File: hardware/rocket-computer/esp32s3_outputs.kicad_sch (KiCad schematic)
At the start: 43 parts, among them J5 Conn_01x04, SW3 R-667995, U11 GD5F2GQ5UEYIGR, U13 W25Q128JVYIQ, U14 479480001, U15 ESP32-S3RH2, U29 TPS22810DRVR, Y1 ABS07-32.768KHZ-T, Y2 ECS-400-10-37B2-CKY-TR

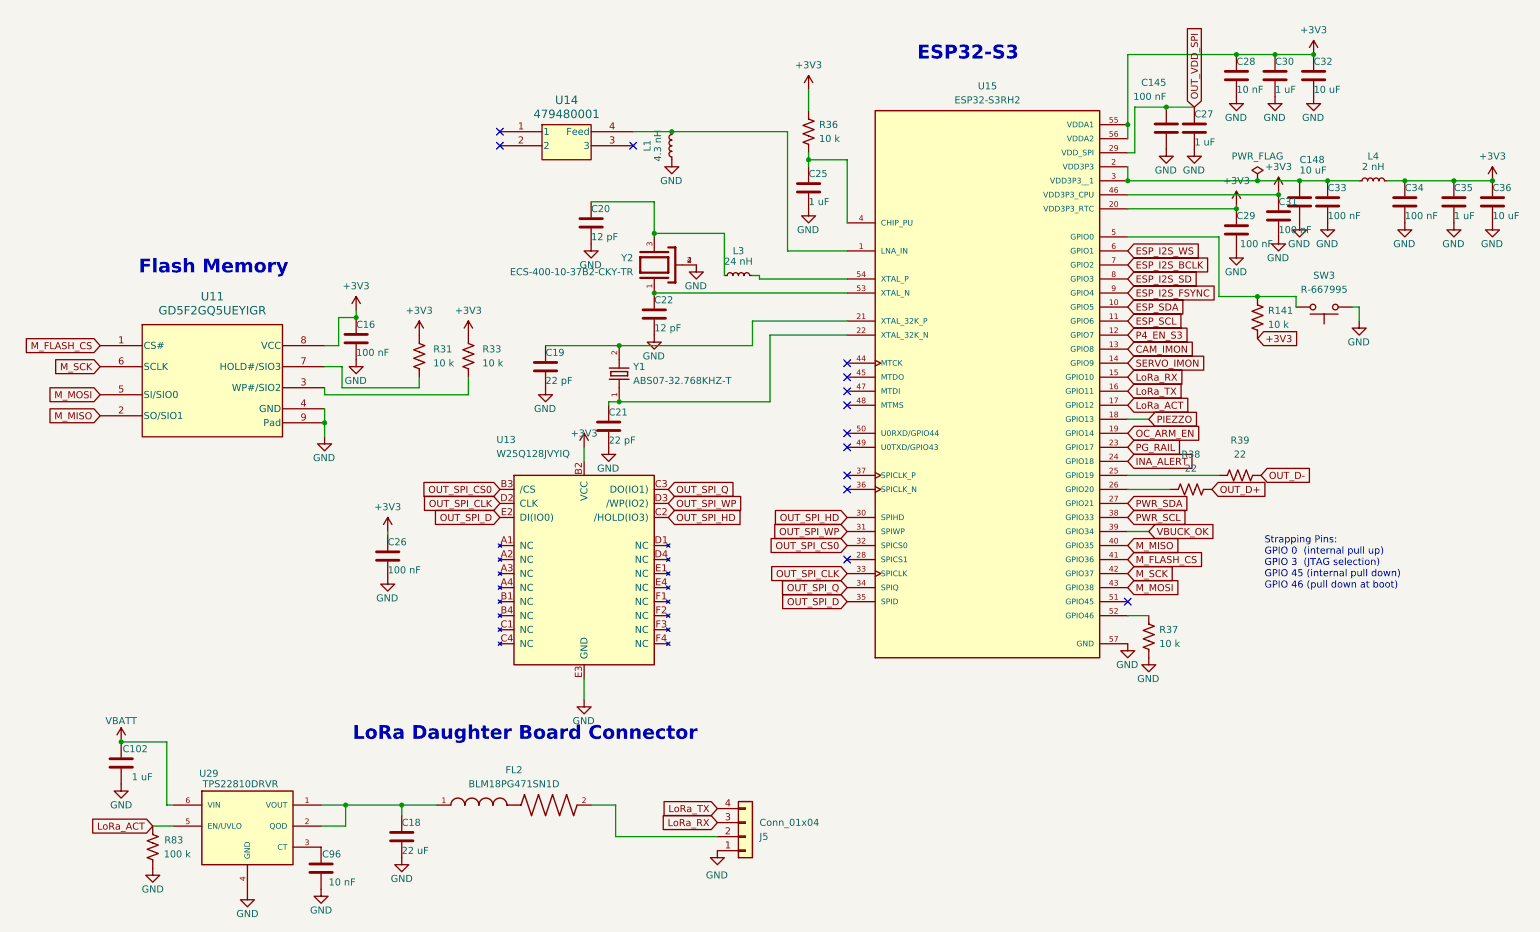
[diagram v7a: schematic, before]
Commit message: hardware(V10): chip antenna in place of the Molex part, buzzer removed, expansion header re-pinned, eight-layer board
Work in progress on the rocket-computer V10, committed so it is not lost. Schematic and
board; placement is under way and routing is not finished, so this is a snapshot of
work in progress rather than a releasable state.

Schematic, against the previous commit: 277 components and 279 nets become 275 and 274.

- The S3 radio front end moves to the mini's network: U22 AANI-CH-0070 with L2 2.2 nH and
  C23 5.1 pF, plus C12 as a do-not-populate shunt. U14 Molex 479480001 and L1 4.3 nH are
  removed.
- The buzzer and its driver are removed: LS1, Q9, R26 and R28. CR1, the flyback across
  the buzzer, goes with them. U15 GPIO13 is now unconnected and is the one electrical-rule
  error on the board; it needs a no-connect flag.
- C56, the 330 uF at the power-mux output, is removed. C45 and C88, both 22 uF, are added
  at the buck input on the far side of L5. The mux output now carries C59 1 uF alone,
  where the V9 and the mini both carry bulk there.
- Expansion header J3 pins 9 to 14 are renumbered so EXP_07 to EXP_12 ascend. P4 GPIO46,
  freed when the magnetometer changed part, leaves the board as EXP_12. Nothing downstream
  follows this yet: board_v9.h, FABRICATION-NOTES B9 and cables.md still describe the old
  pinout.
- R139's pins are swapped with no electrical change.

Board: eight copper layers, 273 footprints inside the outline, updated from the schematic
so it reports no parity items. 124 unconnected items remain, which is the routing still
to do.

Reviewed in hardware/rocket-computer/schematic-review-2026-09-21.md, which carries the
mini-to-V10 parity table. The V10-only power blocks, the document sweep and placement were
not reviewed.

Co-Authored-By: Claude Opus 5 <noreply@anthropic.com>
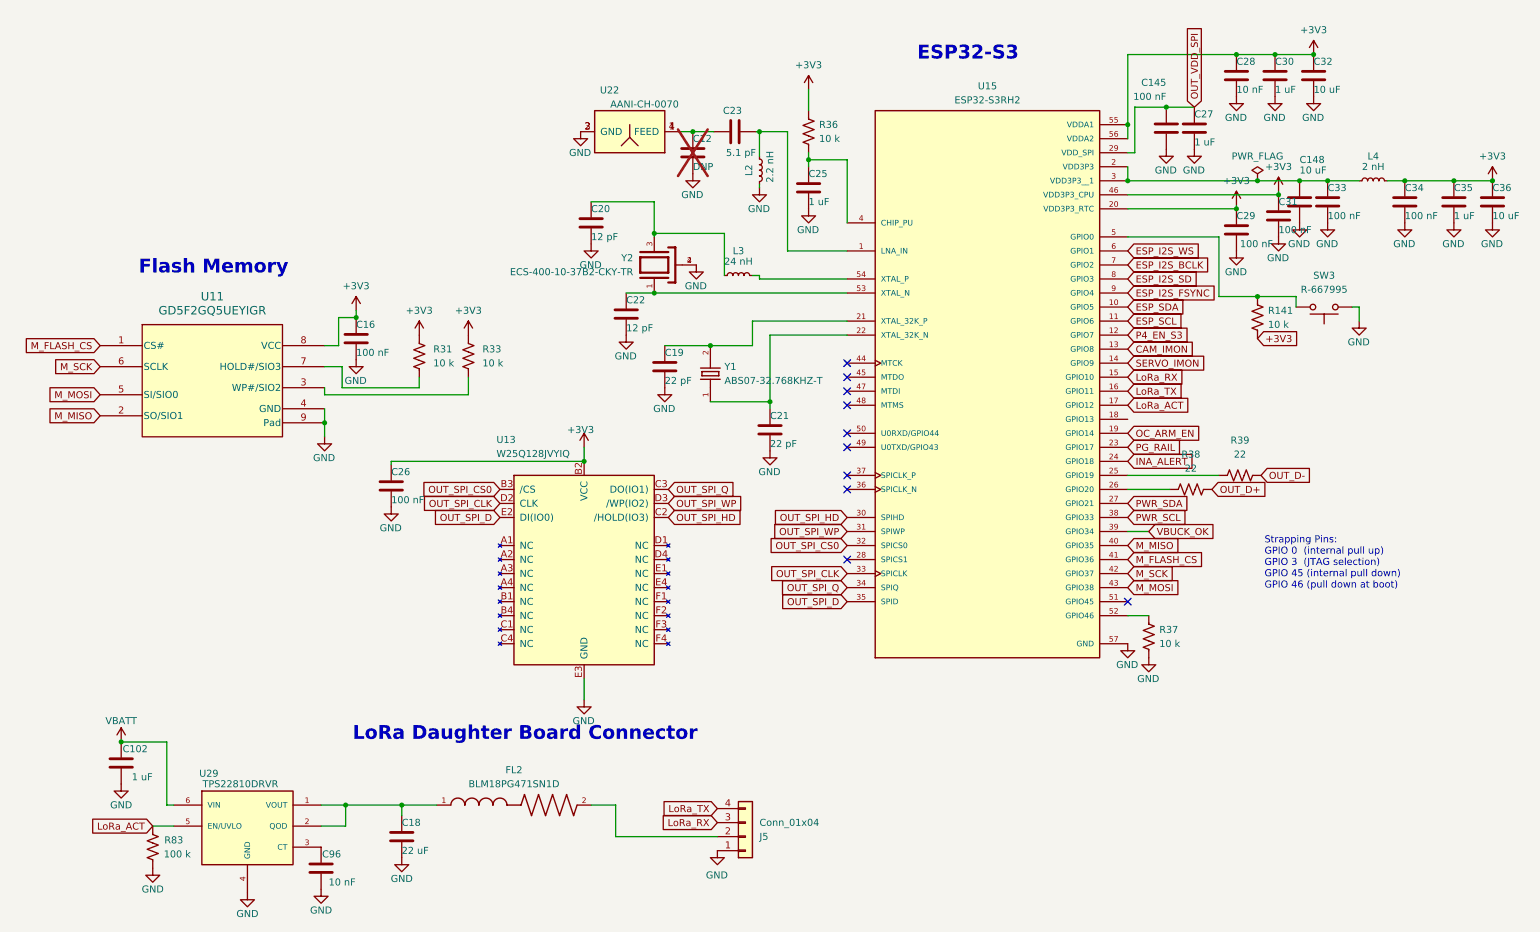
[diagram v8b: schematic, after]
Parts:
- removed L1: 4.3 nH, Inductor_SMD:L_0402_1005Metric, symbol Device:L_Small
- removed U14: 479480001, Footprints:ANT_47948-0001_MOL, symbol Custom:479480001
- added C12: DNP, Capacitor_SMD:C_0402_1005Metric, symbol Device:C
- added C23: 5.1 pF, Capacitor_SMD:C_0402_1005Metric, symbol Device:C
- added L2: 2.2 nH, Inductor_SMD:L_0402_1005Metric, symbol Device:L_Small
- added U22: AANI-CH-0070, Footprints:ANT_AANI-CH-0070_ABR, symbol Custom:AANI-CH-0070
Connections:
- net GND: now also C12.2, L2.2, U22.2 (GND), U22.3 (GND)
- net at U15.1 (LNA_IN): now also C23.2, L2.1
- net PIEZZO: no longer names the net of U15.18 (GPIO13)
- new net: C12.1, C23.1, U22.1 (FEED), U22.4 (FEED)
- no-connect marks 13 -> 10
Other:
- moved on the sheet: C19, C21, C22, C26, Y1
